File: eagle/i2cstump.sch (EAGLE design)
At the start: 21 parts, among them IC1 ATTINY85, IC2 REG1117, J1 I2C-5V, J2 I2C-3V3, Q1 220mA/50V/3.5Ω, Q2 220mA/50V/3.5Ω, X1 USBPCB

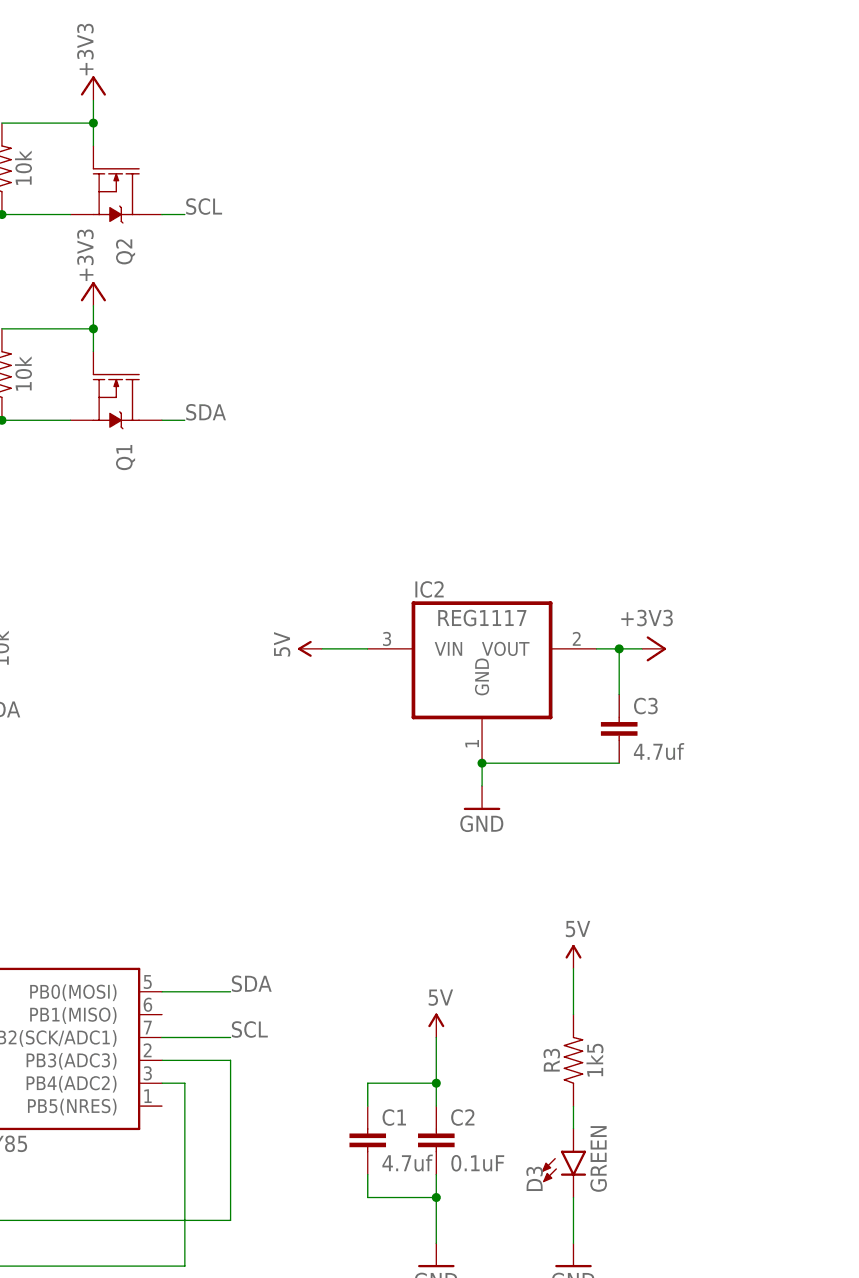
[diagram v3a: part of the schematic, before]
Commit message: Version 2.0
Now with ICSP touchpoints at the bottom so I can flash the AVR.
Also placed tantalum cap C3 (4.uF) on the output of the AM1117.
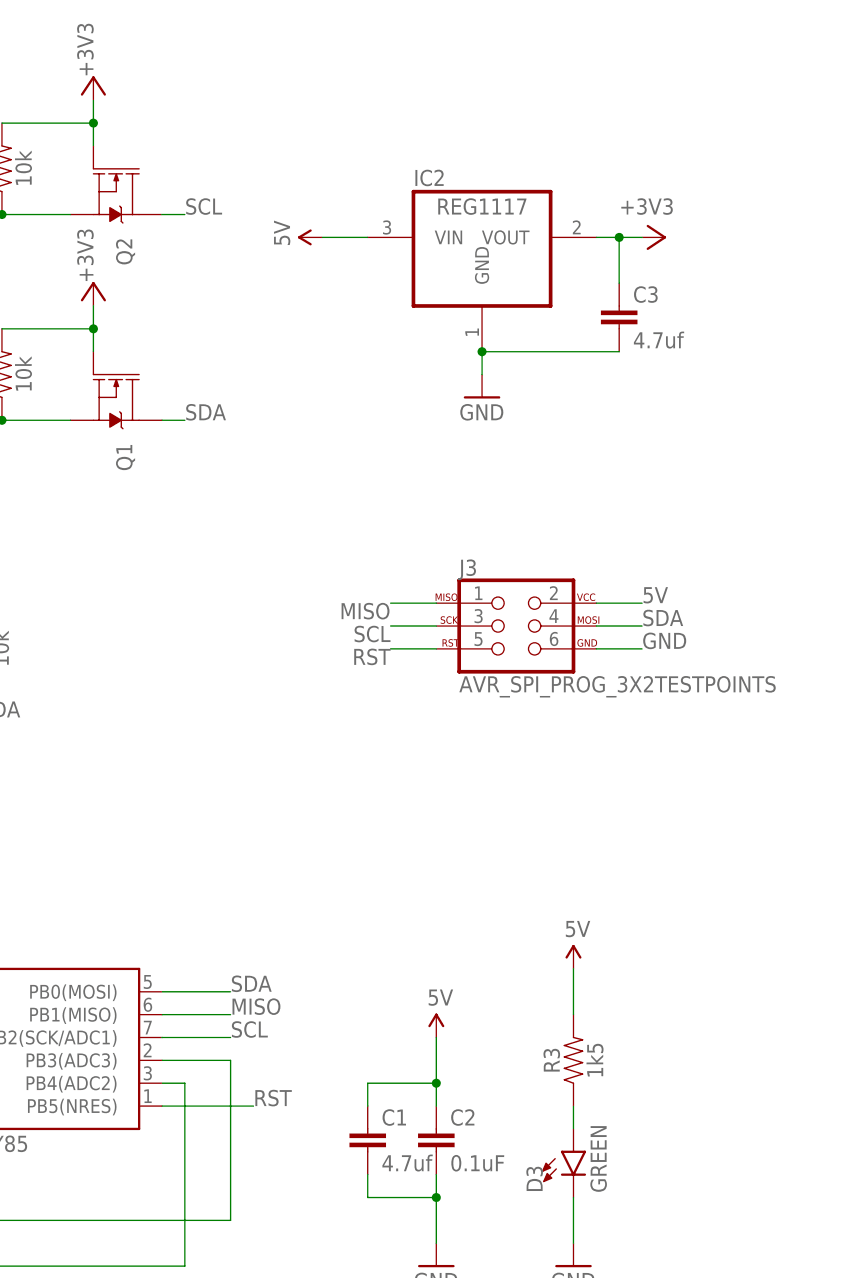
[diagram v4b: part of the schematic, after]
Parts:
- added J3: AVR_SPI_PROG_3X2TESTPOINTS, SparkFun-Connectors:AVR_SPI_PROG_3X2TESTPOINTS
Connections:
- new net MISO: IC1.PB1(MISO), J3.1
- new net RST: IC1.PB5(NRES), J3.5
- net 5V: now also J3.2
- net GND: now also J3.6
- net SCL: now also J3.3
- net SDA: now also J3.4
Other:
- moved on the sheet: C3, IC2
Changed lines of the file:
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@@
 <part name="GND8" library="SparkFun" deviceset="GND" device=""/>
 <part name="C3" library="SparkFun" deviceset="CAP" device="0805" value="4.7uf"/>
+<part name="J3" library="SparkFun-Connectors" library_urn="urn:adsk.eagle:library:513" deviceset="AVR_SPI_PROG_3X2" device="TESTPOINTS" package3d_urn="urn:adsk.eagle:package:38008/1"/>
 </parts>
 <sheets>
@@
 <attribute name="VALUE" x="30.48" y="73.66" size="1.778" layer="96"/>
 </instance>
-<instance part="IC2" gate="G$1" x="129.54" y="83.82" smashed="yes">
-<attribute name="NAME" x="121.92" y="89.535" size="1.778" layer="95" ratio="10"/>
-<attribute name="VALUE" x="124.46" y="86.36" size="1.778" layer="96" ratio="10"/>
-</instance>
-<instance part="U$6" gate="G$1" x="111.76" y="83.82" smashed="yes" rot="R90">
-<attribute name="VALUE" x="108.204" y="82.804" size="1.778" layer="96" rot="R90"/>
-</instance>
-<instance part="+3V1" gate="G$1" x="149.86" y="83.82" smashed="yes" rot="R270">
-<attribute name="VALUE" x="144.78" y="86.36" size="1.778" layer="96"/>
-</instance>
-<instance part="GND5" gate="1" x="129.54" y="66.04" smashed="yes">
-<attribute name="VALUE" x="127" y="63.5" size="1.778" layer="96"/>
+<instance part="IC2" gate="G$1" x="129.54" y="129.54" smashed="yes">
+<attribute name="NAME" x="121.92" y="135.255" size="1.778" layer="95" ratio="10"/>
+<attribute name="VALUE" x="124.46" y="132.08" size="1.778" layer="96" ratio="10"/>
+</instance>
+<instance part="U$6" gate="G$1" x="111.76" y="129.54" smashed="yes" rot="R90">
+<attribute name="VALUE" x="108.204" y="128.524" size="1.778" layer="96" rot="R90"/>
+</instance>
+<instance part="+3V1" gate="G$1" x="149.86" y="129.54" smashed="yes" rot="R270">
+<attribute name="VALUE" x="144.78" y="132.08" size="1.778" layer="96"/>
+</instance>
+<instance part="GND5" gate="1" x="129.54" y="111.76" smashed="yes">
+<attribute name="VALUE" x="127" y="109.22" size="1.778" layer="96"/>
 </instance>
 <instance part="J2" gate="J1" x="20.32" y="121.92" smashed="yes">
@@
 <attribute name="VALUE" x="137.16" y="12.7" size="1.778" layer="96"/>
 </instance>
-<instance part="C3" gate="G$1" x="144.78" y="73.66" smashed="yes">
-<attribute name="NAME" x="146.304" y="76.581" size="1.778" layer="95"/>
-<attribute name="VALUE" x="146.304" y="71.501" size="1.778" layer="96"/>
+<instance part="C3" gate="G$1" x="144.78" y="119.38" smashed="yes">
+<attribute name="NAME" x="146.304" y="122.301" size="1.778" layer="95"/>
+<attribute name="VALUE" x="146.304" y="117.221" size="1.778" layer="96"/>
+</instance>
+<instance part="J3" gate="G$1" x="132.08" y="86.36" smashed="yes">
+<attribute name="NAME" x="127" y="91.948" size="1.778" layer="95" font="vector"/>
+<attribute name="VALUE" x="127" y="78.994" size="1.778" layer="96" font="vector"/>
 </instance>
 </instances>
@@
 <pinref part="IC2" gate="G$1" pin="GND"/>
 <pinref part="GND5" gate="1" pin="GND"/>
-<wire x1="129.54" y1="71.12" x2="129.54" y2="68.58" width="0.1524" layer="91"/>
+<wire x1="129.54" y1="116.84" x2="129.54" y2="114.3" width="0.1524" layer="91"/>
 <pinref part="C3" gate="G$1" pin="2"/>
-<wire x1="144.78" y1="71.12" x2="129.54" y2="71.12" width="0.1524" layer="91"/>
-<junction x="129.54" y="71.12"/>
+<wire x1="144.78" y1="116.84" x2="129.54" y2="116.84" width="0.1524" layer="91"/>
+<junction x="129.54" y="116.84"/>
 </segment>
 <segment>
@@
 <pinref part="GND8" gate="1" pin="GND"/>
 <wire x1="139.7" y1="22.86" x2="139.7" y2="17.78" width="0.1524" layer="91"/>
+</segment>
+<segment>
+<pinref part="J3" gate="G$1" pin="6"/>
+<wire x1="142.24" y1="83.82" x2="147.32" y2="83.82" width="0.1524" layer="91"/>
+<label x="147.32" y="83.82" size="1.778" layer="95"/>
 </segment>
 </net>
@@
 <pinref part="IC2" gate="G$1" pin="VIN"/>
 <pinref part="U$6" gate="G$1" pin="5V"/>
-<wire x1="116.84" y1="83.82" x2="111.76" y2="83.82" width="0.1524" layer="91"/>
+<wire x1="116.84" y1="129.54" x2="111.76" y2="129.54" width="0.1524" layer="91"/>
 </segment>
 <segment>
@@
 <junction x="68.58" y="88.9"/>
 </segment>
+<segment>
+<pinref part="J3" gate="G$1" pin="2"/>
+<wire x1="142.24" y1="88.9" x2="147.32" y2="88.9" width="0.1524" layer="91"/>
+<label x="147.32" y="88.9" size="1.778" layer="95"/>
+</segment>
 </net>
 <net name="N$1" class="0">
@@
 <label x="73.66" y="76.2" size="1.778" layer="95"/>
 </segment>
+<segment>
+<pinref part="J3" gate="G$1" pin="4"/>
+<wire x1="142.24" y1="86.36" x2="147.32" y2="86.36" width="0.1524" layer="91"/>
+<label x="147.32" y="86.36" size="1.778" layer="95"/>
+</segment>
 </net>
 <net name="N$6" class="0">
@@
 <label x="63.5" y="76.2" size="1.778" layer="95"/>
 </segment>
+<segment>
+<pinref part="J3" gate="G$1" pin="3"/>
+<wire x1="124.46" y1="86.36" x2="119.38" y2="86.36" width="0.1524" layer="91"/>
+<label x="119.38" y="86.36" size="1.778" layer="95" rot="R180"/>
+</segment>
 </net>
 <net name="+3V3" class="0">
@@
 <pinref part="+3V1" gate="G$1" pin="+3V3"/>
 <pinref part="IC2" gate="G$1" pin="VOUT"/>
-<wire x1="147.32" y1="83.82" x2="144.78" y2="83.82" width="0.1524" layer="91"/>
+<wire x1="147.32" y1="129.54" x2="144.78" y2="129.54" width="0.1524" layer="91"/>
 <pinref part="C3" gate="G$1" pin="1"/>
-<wire x1="144.78" y1="83.82" x2="142.24" y2="83.82" width="0.1524" layer="91"/>
-<wire x1="144.78" y1="78.74" x2="144.78" y2="83.82" width="0.1524" layer="91"/>
-<junction x="144.78" y="83.82"/>
+<wire x1="144.78" y1="129.54" x2="142.24" y2="129.54" width="0.1524" layer="91"/>
+<wire x1="144.78" y1="124.46" x2="144.78" y2="129.54" width="0.1524" layer="91"/>
+<junction x="144.78" y="129.54"/>
 </segment>
 <segment>
@@
 </segment>
 </net>
+<net name="RST" class="0">
+<segment>
+<pinref part="J3" gate="G$1" pin="5"/>
+<wire x1="124.46" y1="83.82" x2="119.38" y2="83.82" width="0.1524" layer="91"/>
+<label x="119.38" y="83.82" size="1.778" layer="95" rot="R180"/>
+</segment>
+<segment>
+<pinref part="IC1" gate="G$1" pin="PB5(NRES)"/>
+<wire x1="93.98" y1="33.02" x2="104.14" y2="33.02" width="0.1524" layer="91"/>
+<label x="104.14" y="33.02" size="1.778" layer="95"/>
+</segment>
+</net>
+<net name="MISO" class="0">
+<segment>
+<pinref part="J3" gate="G$1" pin="1"/>
+<wire x1="124.46" y1="88.9" x2="119.38" y2="88.9" width="0.1524" layer="91"/>
+<label x="119.38" y="88.9" size="1.778" layer="95" rot="R180"/>
+</segment>
+<segment>
+<pinref part="IC1" gate="G$1" pin="PB1(MISO)"/>
+<wire x1="93.98" y1="43.18" x2="101.6" y2="43.18" width="0.1524" layer="91"/>
+<label x="101.6" y="43.18" size="1.778" layer="95"/>
+</segment>
+</net>

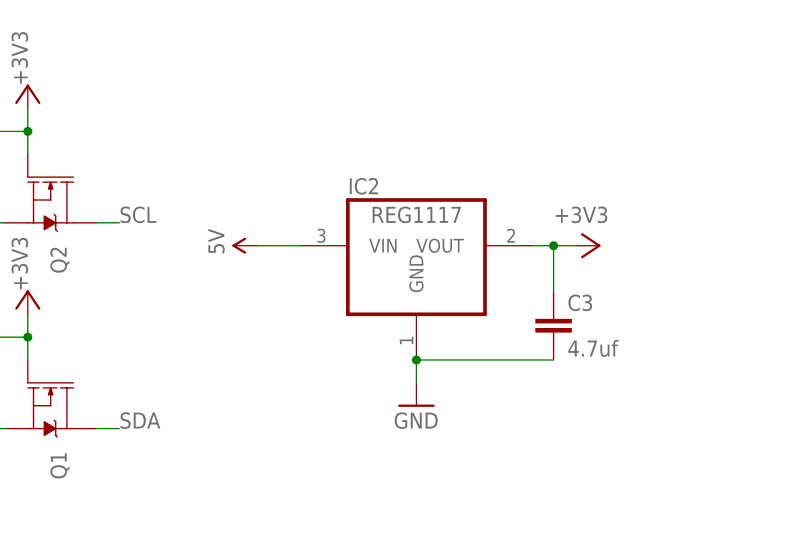
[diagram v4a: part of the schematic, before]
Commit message: Version 3.0 -- with 3mm screwhole in the center. Aligned J1/J2 to be 0.76mm from the edges. Replaced bulky AM1117 (SOT223) with a MCP1700 (SOT23)
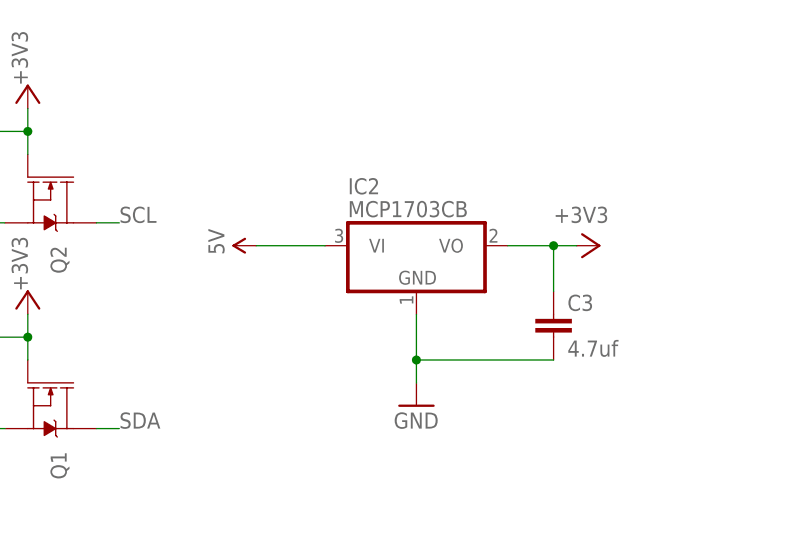
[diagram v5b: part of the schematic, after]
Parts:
- IC2: value REG1117 -> MCP1703CB; device burr-brown:REG1117 -> linear:MCP1703CB
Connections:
- net +3V3: now also IC2.VO; no longer IC2.VOUT
- net 5V: now also IC2.VI; no longer IC2.VIN
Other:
- moved on the sheet: IC2
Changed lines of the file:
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@@
 <part name="U$4" library="SparkFun" deviceset="5V" device=""/>
 <part name="GND4" library="SparkFun" deviceset="GND" device=""/>
-<part name="IC2" library="burr-brown" library_urn="urn:adsk.eagle:library:111" deviceset="REG1117" device="" package3d_urn="urn:adsk.eagle:package:4940/1"/>
 <part name="U$6" library="SparkFun" deviceset="5V" device=""/>
 <part name="+3V1" library="supply1" library_urn="urn:adsk.eagle:library:371" deviceset="+3V3" device=""/>
@@
 <part name="C3" library="SparkFun" deviceset="CAP" device="0805" value="4.7uf"/>
 <part name="J3" library="SparkFun-Connectors" library_urn="urn:adsk.eagle:library:513" deviceset="AVR_SPI_PROG_3X2" device="TESTPOINTS" package3d_urn="urn:adsk.eagle:package:38008/1"/>
+<part name="IC2" library="linear" library_urn="urn:adsk.eagle:library:262" deviceset="MCP1703" device="CB" package3d_urn="urn:adsk.eagle:package:16489/2"/>
 </parts>
 <sheets>
@@
 <attribute name="VALUE" x="30.48" y="73.66" size="1.778" layer="96"/>
 </instance>
-<instance part="IC2" gate="G$1" x="129.54" y="129.54" smashed="yes">
-<attribute name="NAME" x="121.92" y="135.255" size="1.778" layer="95" ratio="10"/>
-<attribute name="VALUE" x="124.46" y="132.08" size="1.778" layer="96" ratio="10"/>
-</instance>
 <instance part="U$6" gate="G$1" x="111.76" y="129.54" smashed="yes" rot="R90">
 <attribute name="VALUE" x="108.204" y="128.524" size="1.778" layer="96" rot="R90"/>
@@
 <attribute name="NAME" x="127" y="91.948" size="1.778" layer="95" font="vector"/>
 <attribute name="VALUE" x="127" y="78.994" size="1.778" layer="96" font="vector"/>
+</instance>
+<instance part="IC2" gate="G$1" x="129.54" y="129.54" smashed="yes">
+<attribute name="NAME" x="121.92" y="135.255" size="1.778" layer="95"/>
+<attribute name="VALUE" x="121.92" y="132.715" size="1.778" layer="96"/>
 </instance>
 </instances>
@@
 </segment>
 <segment>
-<pinref part="IC2" gate="G$1" pin="GND"/>
 <pinref part="GND5" gate="1" pin="GND"/>
 <wire x1="129.54" y1="116.84" x2="129.54" y2="114.3" width="0.1524" layer="91"/>
 <pinref part="C3" gate="G$1" pin="2"/>
 <wire x1="144.78" y1="116.84" x2="129.54" y2="116.84" width="0.1524" layer="91"/>
+<pinref part="IC2" gate="G$1" pin="GND"/>
+<wire x1="129.54" y1="116.84" x2="129.54" y2="121.92" width="0.1524" layer="91"/>
 <junction x="129.54" y="116.84"/>
 </segment>
@@
 </segment>
 <segment>
-<pinref part="IC2" gate="G$1" pin="VIN"/>
 <pinref part="U$6" gate="G$1" pin="5V"/>
-<wire x1="116.84" y1="129.54" x2="111.76" y2="129.54" width="0.1524" layer="91"/>
+<wire x1="119.38" y1="129.54" x2="111.76" y2="129.54" width="0.1524" layer="91"/>
+<pinref part="IC2" gate="G$1" pin="VI"/>
 </segment>
 <segment>
@@
 <segment>
 <pinref part="+3V1" gate="G$1" pin="+3V3"/>
-<pinref part="IC2" gate="G$1" pin="VOUT"/>
 <wire x1="147.32" y1="129.54" x2="144.78" y2="129.54" width="0.1524" layer="91"/>
 <pinref part="C3" gate="G$1" pin="1"/>
-<wire x1="144.78" y1="129.54" x2="142.24" y2="129.54" width="0.1524" layer="91"/>
 <wire x1="144.78" y1="124.46" x2="144.78" y2="129.54" width="0.1524" layer="91"/>
 <junction x="144.78" y="129.54"/>
-</segment>
-<segment>
+<pinref part="IC2" gate="G$1" pin="VO"/>
+<wire x1="139.7" y1="129.54" x2="144.78" y2="129.54" width="0.1524" layer="91"/>
+</segment>
+<segment>
